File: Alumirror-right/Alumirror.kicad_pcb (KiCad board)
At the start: 2 copper layers, 139.7 x 88.9 mm, 67 parts, among them J2 USB_C_Receptacle_USB2.0_16P_2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, J4 USB_C_Receptacle_USB2.0_16P_2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, K11 PG1350, K12 PG1350, K13 PG1350, K14 PG1350, K15 PG1350, K16 PG1350, K21 PG1350, K22 PG1350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

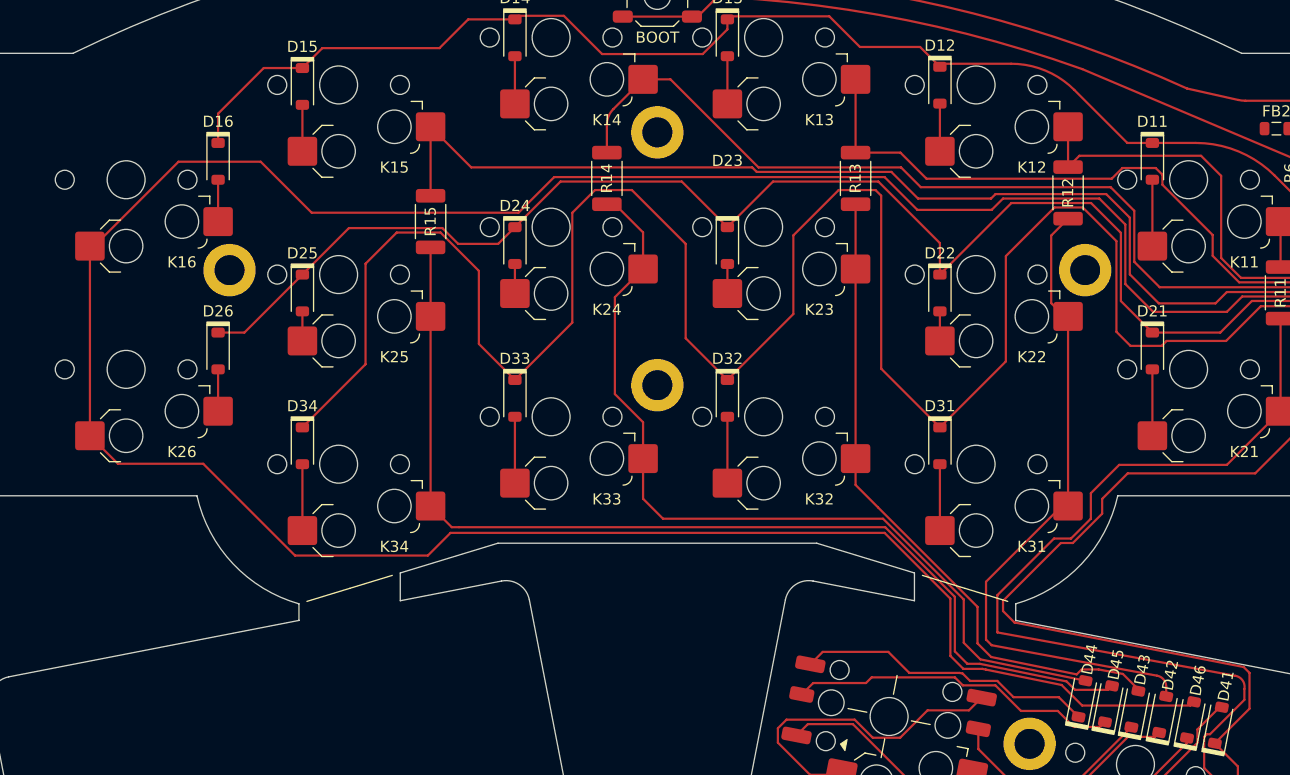
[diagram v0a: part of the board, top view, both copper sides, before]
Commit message: Updated Row 3 diode placement
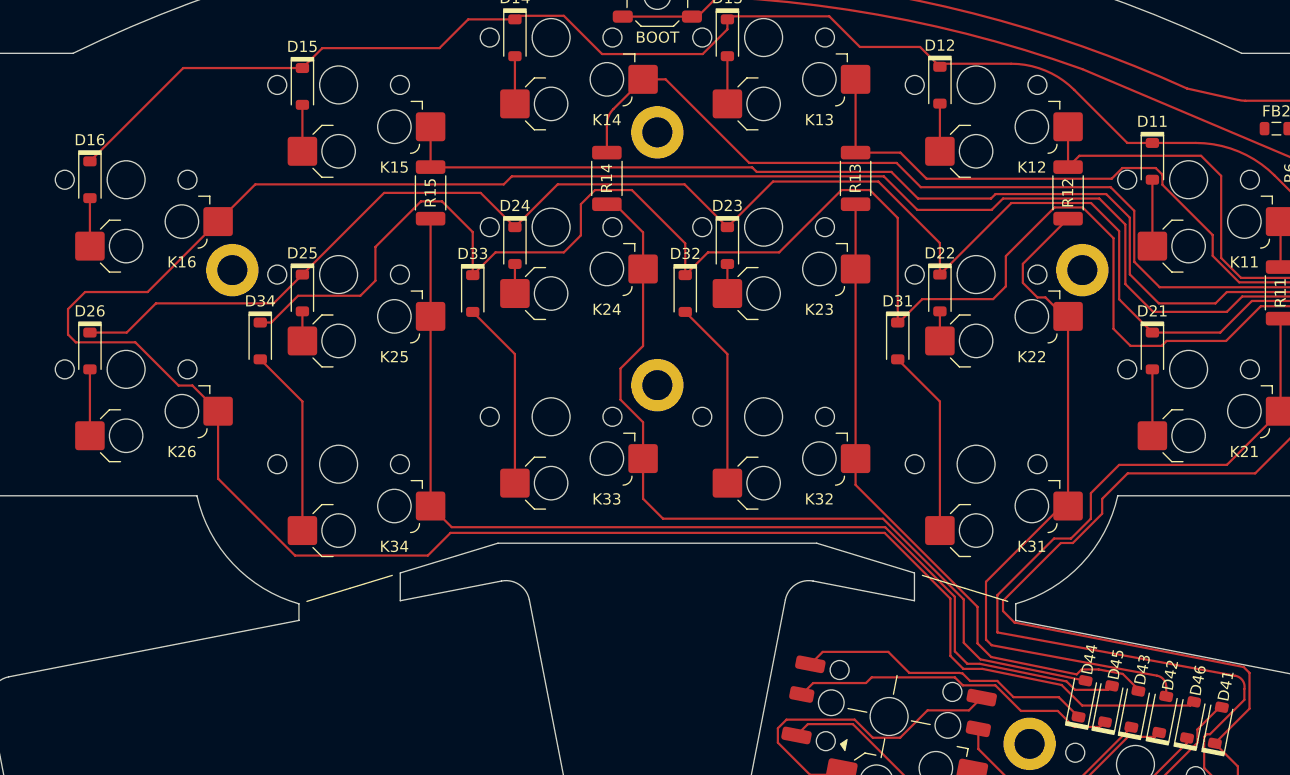
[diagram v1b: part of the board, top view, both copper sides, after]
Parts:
- moved D16 11.6 mm to (101.5, 52.4)
- moved D26 11.5 mm to (101.5, 67.8)
- moved D31 10.1 mm to (173.9, 66.9)
- moved D32 10.1 mm to (154.9, 62.6)
- moved D33 10.1 mm to (135.8, 62.6)
- moved D34 10.1 mm to (116.8, 66.9)
- moved R15 2.57 mm to (132.1, 53.6)
- moved H1 0.25 mm to (114.3, 60.5)
- moved H4 0.25 mm to (190.5, 60.5)
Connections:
- K16 pad 1: Net-(D16-A) -> Col6
- K16 pad 2: Col6 -> Net-(D16-A)
- K26 pad 1: Net-(D26-A) -> Col6
- K26 pad 2: Col6 -> Net-(D26-A)
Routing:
- net Row3: track 192.5 -> 147.1 mm
- net Row2: track 126.7 -> 139.4 mm
- net Net-(D33-A): track 5.95 -> 16.9 mm
- net Net-(D32-A): track 5.95 -> 16.9 mm
- net Net-(D31-A): track 5.95 -> 16.9 mm
- net Net-(D34-A): track 5.95 -> 16.9 mm
- net Row1: track 117.3 -> 127.9 mm
- net Col6: track 256.9 -> 252.0 mm
- net Col5: track 96.4 -> 92.4 mm
- net Col5T: track 93.6 -> 96.2 mm
- net Net-(D26-A): track 3.75 -> 5.95 mm
- net Col2T: track 60.7 -> 62.7 mm
- net Col4T: track 78.7 -> 77.2 mm
- net Net-(D16-A): track 3.35 -> 4.30 mm

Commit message: Various tweaks
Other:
- outline, holes or cut-outs redrawn
- board text removed: "LED"
